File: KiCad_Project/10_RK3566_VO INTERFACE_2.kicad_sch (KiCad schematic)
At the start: 3 parts

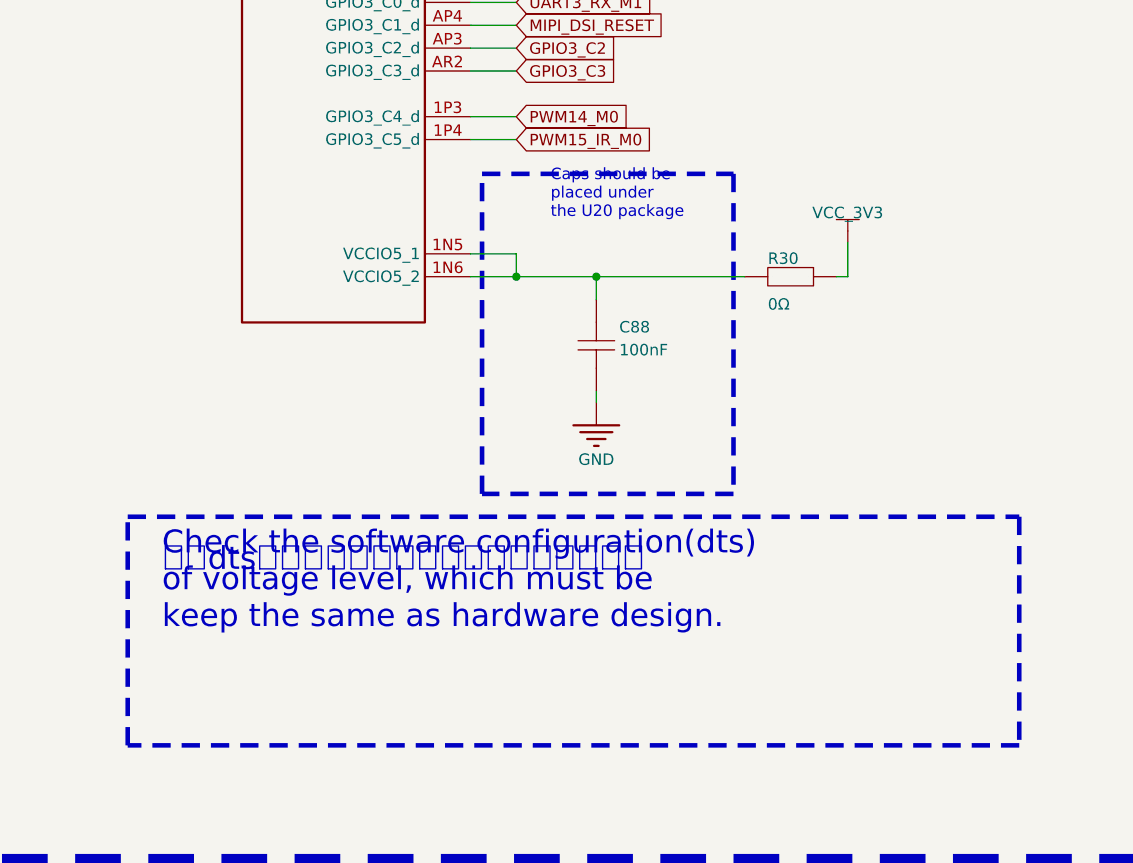
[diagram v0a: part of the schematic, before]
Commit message: Update additional PCBs
Add WIFI PCB to get best antenna
Add Display Debbugger to get interface pinout
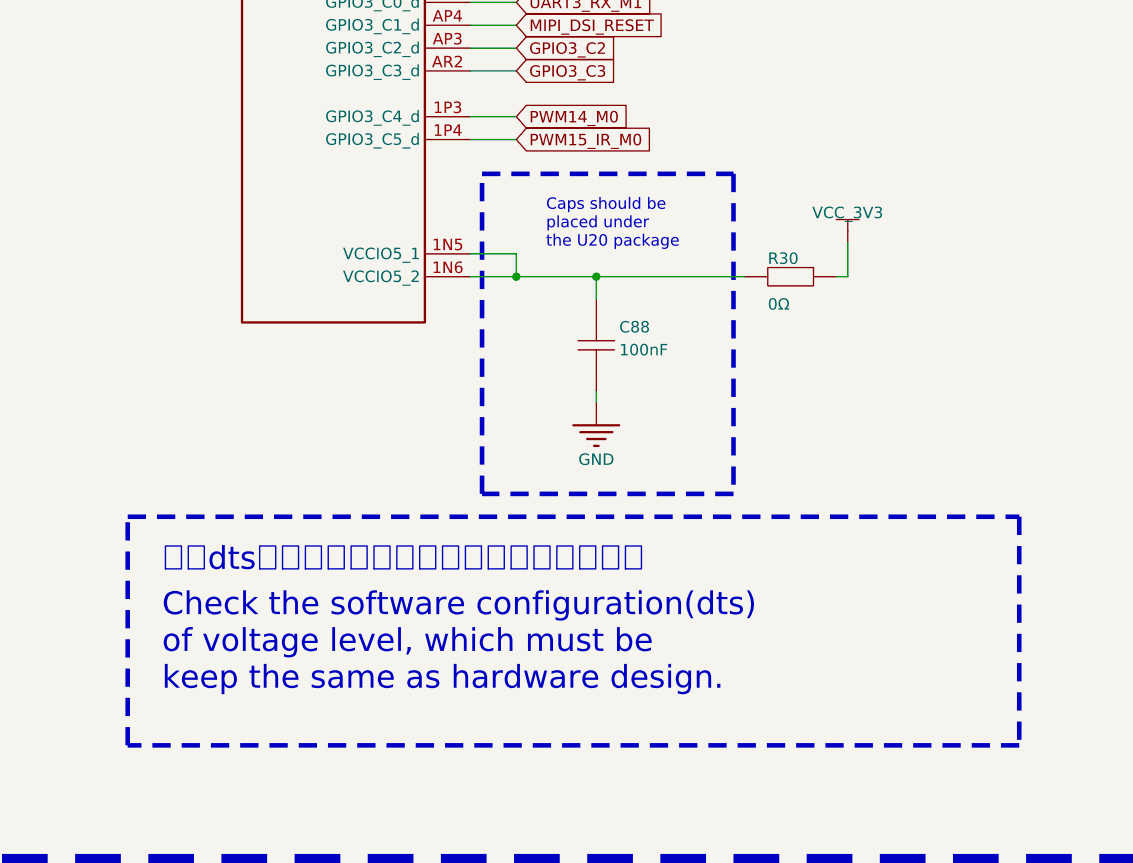
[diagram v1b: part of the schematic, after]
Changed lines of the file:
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@@
 	(text "Caps should be \nplaced under \nthe U20 package"
 		(exclude_from_sim no)
-		(at 209.55 166.37 0)
+		(at 209.042 169.672 0)
 		(effects
 			(font
@@
 	(text "Check the software configuration(dts)\nof voltage level, which must be\nkeep the same as hardware design."
 		(exclude_from_sim no)
-		(at 166.37 212.09 0)
+		(at 166.37 218.948 0)
 		(effects
 			(font
